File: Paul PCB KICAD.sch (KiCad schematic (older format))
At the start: 19 parts

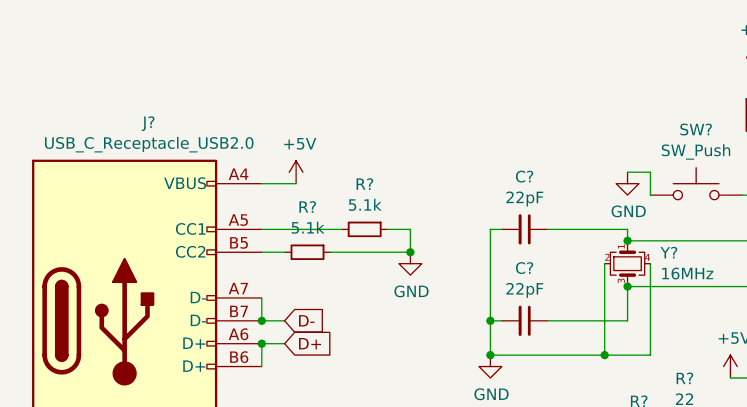
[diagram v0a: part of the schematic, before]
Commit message: Fixed +5V for USB
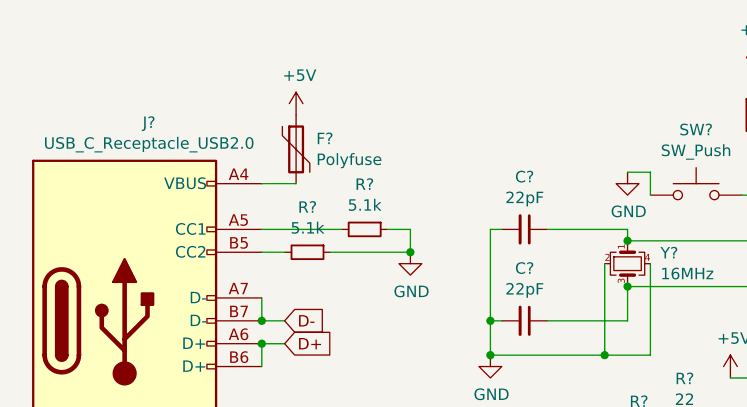
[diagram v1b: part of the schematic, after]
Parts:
- added F?: Polyfuse, symbol Device:Polyfuse
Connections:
- net +5V: now also F?.1; no longer J?.A4 (VBUS), J?.A9 (VBUS), J?.B4 (VBUS), J?.B9 (VBUS)
- new net: F?.2, J?.A4 (VBUS), J?.A9 (VBUS), J?.B4 (VBUS), J?.B9 (VBUS)
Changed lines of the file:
@@
 L power:+5V #PWR?
 U 1 1 6080295E
-P 1800 2000
-F 0 "#PWR?" H 1800 1850 50  0001 C CNN
-F 1 "+5V" H 1815 2173 50  0000 C CNN
-F 2 "" H 1800 2000 50  0001 C CNN
-F 3 "" H 1800 2000 50  0001 C CNN
-	1    1800 2000
+P 1800 1700
+F 0 "#PWR?" H 1800 1550 50  0001 C CNN
+F 1 "+5V" H 1815 1873 50  0000 C CNN
+F 2 "" H 1800 1700 50  0001 C CNN
+F 3 "" H 1800 1700 50  0001 C CNN
+	1    1800 1700
 	1    0    0    -1
 $EndComp
@@
 Wire Wire Line
 	850  4050 1100 4050
+$Comp
+L Device:Polyfuse F?
+U 1 1 607B6BD8
+P 1800 1850
+F 0 "F?" H 1888 1896 50  0000 L CNN
+F 1 "Polyfuse" H 1888 1805 50  0000 L CNN
+F 2 "" H 1850 1650 50  0001 L CNN
+F 3 "~" H 1800 1850 50  0001 C CNN
+	1    1800 1850
+	1    0    0    -1
+$EndComp
 $EndSCHEMATC

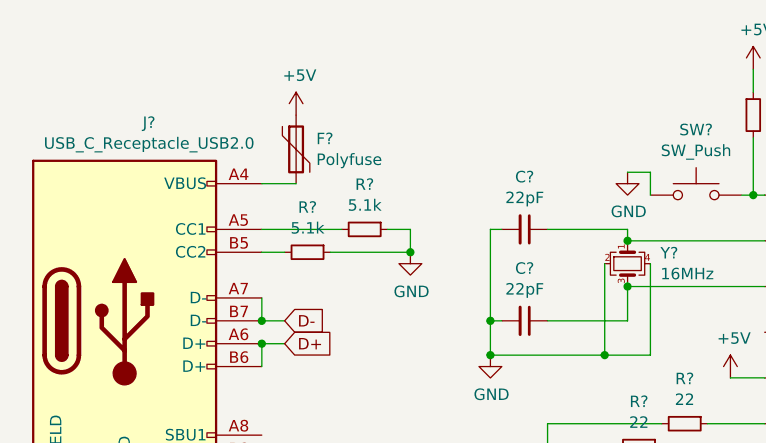
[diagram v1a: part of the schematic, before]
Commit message: Added License and fixed PolyFuse Value
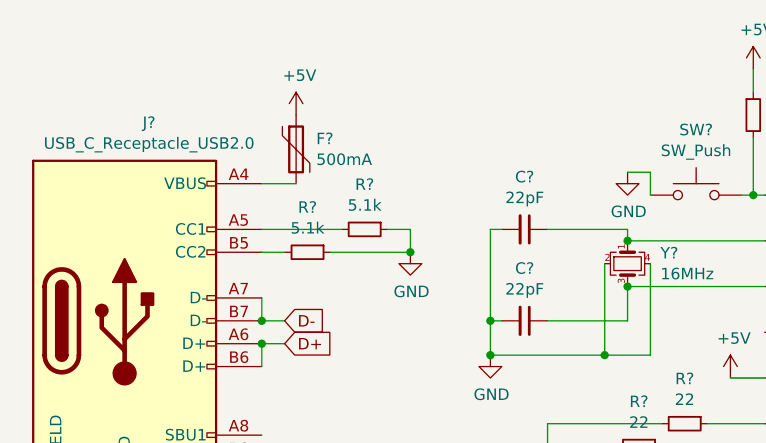
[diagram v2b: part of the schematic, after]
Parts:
- F?: value Polyfuse -> 500mA
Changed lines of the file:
@@
 P 1800 1850
 F 0 "F?" H 1888 1896 50  0000 L CNN
-F 1 "Polyfuse" H 1888 1805 50  0000 L CNN
+F 1 "500mA" H 1888 1805 50  0000 L CNN
 F 2 "" H 1850 1650 50  0001 L CNN
 F 3 "~" H 1800 1850 50  0001 C CNN

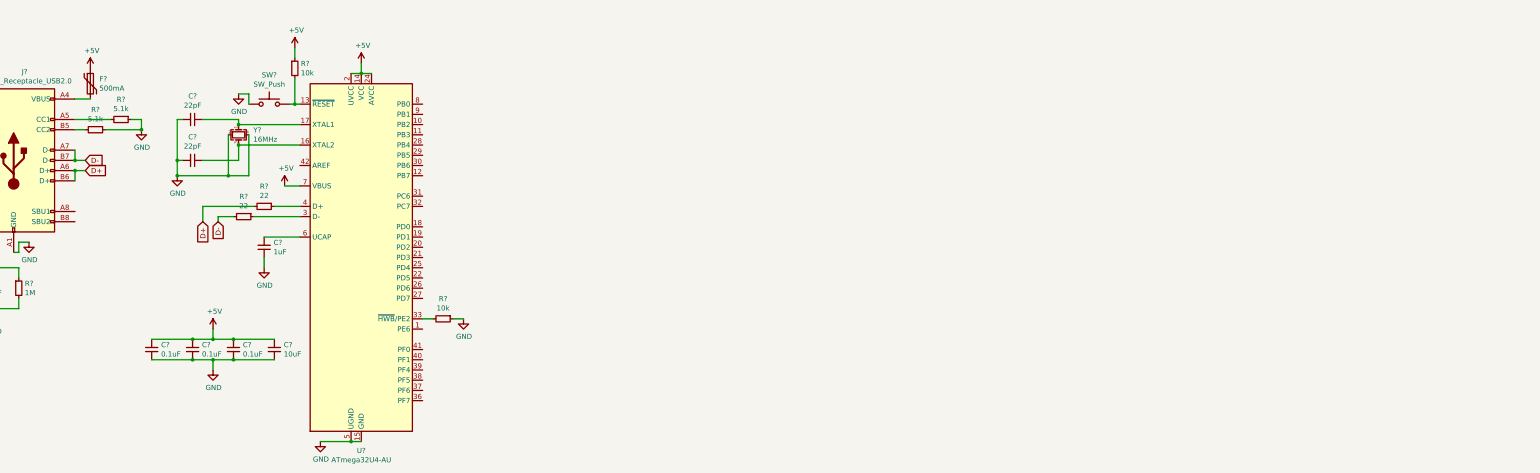
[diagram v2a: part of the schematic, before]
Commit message: Added Switch Layout to Schematic
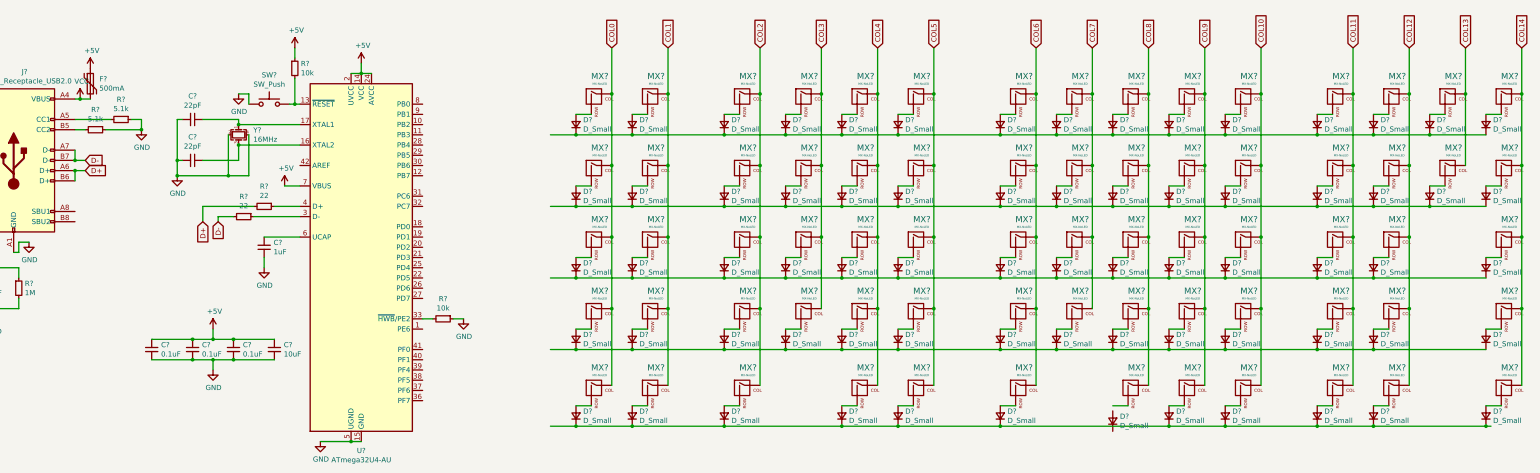
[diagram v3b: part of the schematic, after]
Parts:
- added D? (x70): D_Small, symbol Device:D_Small
- added MX? (x70): MX-NoLED, symbol MX_Alps_Hybrid:MX-NoLED
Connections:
- net VCC: now reaches F?.2, J?.A4 (VBUS), J?.A9 (VBUS), J?.B4 (VBUS), J?.B9 (VBUS)
- new net: D?.2 (A), MX?.2 (ROW) (x69)
- new net: D?.1 (K), D?.1 (K), D?.1 (K), D?.1 (K), D?.1 (K), D?.1 (K), D?.1 (K), D?.1 (K), D?.1 (K), D?.1 (K), D?.1 (K), D?.1 (K), D?.1 (K), D?.1 (K), D?.1 (K) (x2)
- new net: D?.1 (K), D?.1 (K), D?.1 (K), D?.1 (K), D?.1 (K), D?.1 (K), D?.1 (K), D?.1 (K), D?.1 (K), D?.1 (K), D?.1 (K), D?.1 (K), D?.1 (K), D?.1 (K) (x2)
- new net: D?.1 (K), D?.1 (K), D?.1 (K), D?.1 (K), D?.1 (K), D?.1 (K), D?.1 (K), D?.1 (K), D?.1 (K), D?.1 (K), D?.1 (K)
- new net COL0: MX?.1 (COL), MX?.1 (COL), MX?.1 (COL), MX?.1 (COL), MX?.1 (COL)
- new net COL1: MX?.1 (COL), MX?.1 (COL), MX?.1 (COL), MX?.1 (COL), MX?.1 (COL)
- new net COL10: MX?.1 (COL), MX?.1 (COL), MX?.1 (COL), MX?.1 (COL), MX?.1 (COL)
- new net COL11: MX?.1 (COL), MX?.1 (COL), MX?.1 (COL), MX?.1 (COL), MX?.1 (COL)
- new net COL12: MX?.1 (COL), MX?.1 (COL), MX?.1 (COL), MX?.1 (COL), MX?.1 (COL)
- new net COL13: MX?.1 (COL), MX?.1 (COL)
- new net COL14: MX?.1 (COL), MX?.1 (COL), MX?.1 (COL), MX?.1 (COL), MX?.1 (COL)
- new net COL2: MX?.1 (COL), MX?.1 (COL), MX?.1 (COL), MX?.1 (COL), MX?.1 (COL)
- new net COL3: MX?.1 (COL), MX?.1 (COL), MX?.1 (COL), MX?.1 (COL)
- new net COL4: MX?.1 (COL), MX?.1 (COL), MX?.1 (COL), MX?.1 (COL), MX?.1 (COL)
- new net COL5: MX?.1 (COL), MX?.1 (COL), MX?.1 (COL), MX?.1 (COL), MX?.1 (COL)
- new net COL6: MX?.1 (COL), MX?.1 (COL), MX?.1 (COL), MX?.1 (COL), MX?.1 (COL)
- new net COL7: MX?.1 (COL), MX?.1 (COL), MX?.1 (COL), MX?.1 (COL)
- new net COL8: MX?.1 (COL), MX?.1 (COL), MX?.1 (COL), MX?.1 (COL), MX?.1 (COL)
- new net COL9: MX?.1 (COL), MX?.1 (COL), MX?.1 (COL), MX?.1 (COL), MX?.1 (COL)

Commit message: Started Adding Footprints
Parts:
- C1, C2, C3, C4, C5, C6, C7, C8: renamed from C?; footprint (none) -> Capacitor_SMD:C_0805_2012Metric
- D1, D10, D11, D12, D13, D14, D15, D16, D17, D18, D19, D2, D20, D21, D22, D23, D24, D25, D26, D27, D28, D29, D3, D30, D31, D32, D33, D34, D35, D36, D37, D38, D39, D4, D40, D41, D42, D43, D44, D45, D46, D47, D48, D49, D5, D50, D51, D52, D53, D54, D55, D56, D57, D58, D59, D6, D60, D61, D62, D63, D64, D65, D66, D67, D68, D69, D7, D70, D8, D9: renamed from D?; footprint (none) -> Diode_SMD:D_SOD-123
- F1: renamed from F?; footprint (none) -> Fuse:Fuse_1206_3216Metric
- MX1: renamed from MX?; footprint (none) -> MX_Only:MXOnly-1U-Hotswap
- gave numbers to parts that had none: 80
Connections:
- net ROW0: now reaches D1.1 (K), D11.1 (K), D16.1 (K), D20.1 (K), D25.1 (K), D30.1 (K), D35.1 (K), D39.1 (K), D44.1 (K), D49.1 (K), D54.1 (K), D59.1 (K), D6.1 (K), D64.1 (K), D66.1 (K)
- net ROW1: now reaches D12.1 (K), D17.1 (K), D2.1 (K), D21.1 (K), D26.1 (K), D31.1 (K), D36.1 (K), D40.1 (K), D45.1 (K), D50.1 (K), D55.1 (K), D60.1 (K), D65.1 (K), D67.1 (K), D7.1 (K)
- net ROW2: now reaches D13.1 (K), D18.1 (K), D22.1 (K), D27.1 (K), D3.1 (K), D32.1 (K), D37.1 (K), D41.1 (K), D46.1 (K), D51.1 (K), D56.1 (K), D61.1 (K), D68.1 (K), D8.1 (K)
- net ROW3: now reaches D14.1 (K), D19.1 (K), D23.1 (K), D28.1 (K), D33.1 (K), D38.1 (K), D4.1 (K), D42.1 (K), D47.1 (K), D52.1 (K), D57.1 (K), D62.1 (K), D69.1 (K), D9.1 (K)
- net ROW4: now reaches D10.1 (K), D15.1 (K), D24.1 (K), D29.1 (K), D34.1 (K), D48.1 (K), D5.1 (K), D53.1 (K), D58.1 (K), D63.1 (K), D70.1 (K)

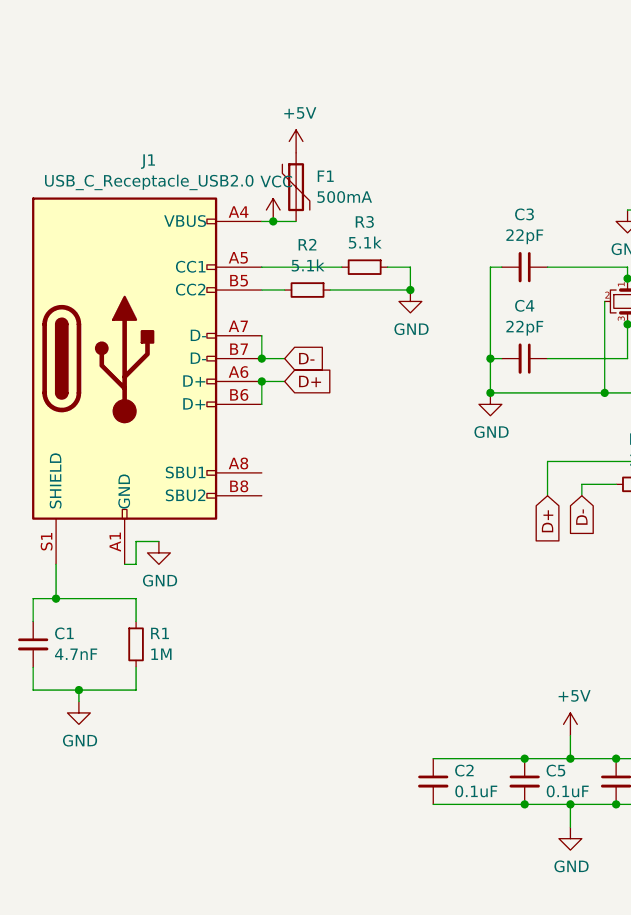
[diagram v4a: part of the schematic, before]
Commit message: Updated USB to 4084 GCT
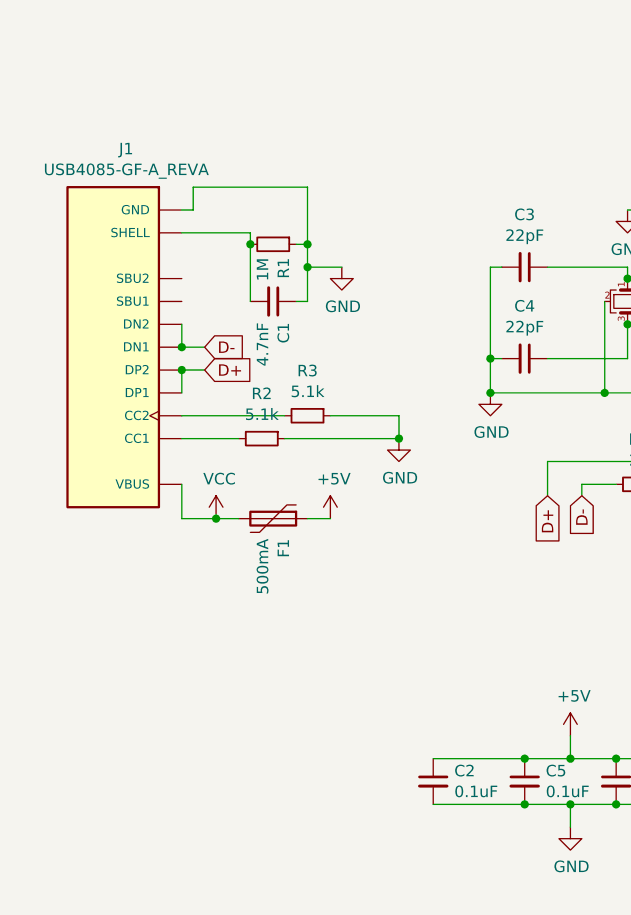
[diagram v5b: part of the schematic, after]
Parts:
- removed J1: USB_C_Receptacle_USB2.0, symbol Connector:USB_C_Receptacle_USB2.0
- added J1: USB4085-GF-A_REVA, 4085 USB Connector GCT:GCT_USB4085-GF-A_REVA, symbol USB4085-GF-A_REVA:USB4085-GF-A_REVA
- R1, R2, R3, R4, R5, R6, R7: footprint (none) -> Resistor_SMD:R_0805_2012Metric
- SW1: footprint (none) -> random-keyboard-parts:SKQG-1155865
- Y1: footprint (none) -> Crystal:Crystal_SMD_3225-4Pin_3.2x2.5mm
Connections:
- net D+: now also J1.A6 (DP1), J1.B6 (DP2)
- net D-: now also J1.A7 (DN1), J1.B7 (DN2)
- net GND: now also C1.1, R1.1, J1.A1 (GND), J1.A12 (GND), J1.B1 (GND), J1.B12 (GND); no longer C1.2, R1.2
- net VCC: now also J1.A4 (VBUS), J1.A9 (VBUS), J1.B4 (VBUS), J1.B9 (VBUS)
- net at R3.2: now also J1.B5 (CC2)
- net at R2.2: now also J1.A5 (CC1)
- new net: C1.2, J1.P1 (SHELL), J1.P2 (SHELL), J1.P3 (SHELL), J1.P4 (SHELL), R1.2
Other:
- moved on the sheet: C1, F1, R1, R2, R3
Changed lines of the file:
@@
 F 0 "R7" V 5054 4150 50  0000 C CNN
 F 1 "10k" V 5145 4150 50  0000 C CNN
-F 2 "" H 5250 4150 50  0001 C CNN
+F 2 "Resistor_SMD:R_0805_2012Metric" H 5250 4150 50  0001 C CNN
 F 3 "~" H 5250 4150 50  0001 C CNN
 	1    5250 4150
@@
 F 0 "R5" V 3304 3050 50  0000 C CNN
 F 1 "22" V 3395 3050 50  0000 C CNN
-F 2 "" H 3500 3050 50  0001 C CNN
+F 2 "Resistor_SMD:R_0805_2012Metric" H 3500 3050 50  0001 C CNN
 F 3 "~" H 3500 3050 50  0001 C CNN
 	1    3500 3050
@@
 F 0 "R4" V 3104 3150 50  0000 C CNN
 F 1 "22" V 3195 3150 50  0000 C CNN
-F 2 "" H 3300 3150 50  0001 C CNN
+F 2 "Resistor_SMD:R_0805_2012Metric" H 3300 3150 50  0001 C CNN
 F 3 "~" H 3300 3150 50  0001 C CNN
 	1    3300 3150
@@
 F 0 "Y1" V 3204 2494 50  0000 L CNN
 F 1 "16MHz" V 3295 2494 50  0000 L CNN
-F 2 "" H 3250 2350 50  0001 C CNN
+F 2 "Crystal:Crystal_SMD_3225-4Pin_3.2x2.5mm" H 3250 2350 50  0001 C CNN
 F 3 "~" H 3250 2350 50  0001 C CNN
 	1    3250 2350
@@
 F 0 "R6" H 3859 1746 50  0000 L CNN
 F 1 "10k" H 3859 1655 50  0000 L CNN
-F 2 "" H 3800 1700 50  0001 C CNN
+F 2 "Resistor_SMD:R_0805_2012Metric" H 3800 1700 50  0001 C CNN
 F 3 "~" H 3800 1700 50  0001 C CNN
 	1    3800 1700
@@
 F 0 "SW1" H 3550 2335 50  0000 C CNN
 F 1 "SW_Push" H 3550 2244 50  0000 C CNN
-F 2 "" H 3550 2250 50  0001 C CNN
+F 2 "random-keyboard-parts:SKQG-1155865" H 3550 2250 50  0001 C CNN
 F 3 "~" H 3550 2250 50  0001 C CNN
 	1    3550 2050
@@
 D-
 $Comp
-L Connector:USB_C_Receptacle_USB2.0 J1
-U 1 1 607E82B6
-P 1050 2600
-F 0 "J1" H 1157 3467 50  0000 C CNN
-F 1 "USB_C_Receptacle_USB2.0" H 1157 3376 50  0000 C CNN
-F 2 "" H 1200 2600 50  0001 C CNN
-F 3 "https://www.usb.org/sites/default/files/documents/usb_type-c.zip" H 1200 2600 50  0001 C CNN
-	1    1050 2600
-	1    0    0    -1
-$EndComp
-$Comp
 L power:GND #PWR0111
 U 1 1 607F76C2
-P 1200 3400
-F 0 "#PWR0111" H 1200 3150 50  0001 C CNN
-F 1 "GND" H 1205 3227 50  0000 C CNN
-F 2 "" H 1200 3400 50  0001 C CNN
-F 3 "" H 1200 3400 50  0001 C CNN
-	1    1200 3400
+P 2000 2200
+F 0 "#PWR0111" H 2000 1950 50  0001 C CNN
+F 1 "GND" H 2005 2027 50  0000 C CNN
+F 2 "" H 2000 2200 50  0001 C CNN
+F 3 "" H 2000 2200 50  0001 C CNN
+	1    2000 2200
 	1    0    0    -1
 $EndComp
@@
 L power:GND #PWR0112
 U 1 1 607F7AE7
-P 2300 2300
-F 0 "#PWR0112" H 2300 2050 50  0001 C CNN
-F 1 "GND" H 2305 2127 50  0000 C CNN
-F 2 "" H 2300 2300 50  0001 C CNN
-F 3 "" H 2300 2300 50  0001 C CNN
-	1    2300 2300
+P 2250 2950
+F 0 "#PWR0112" H 2250 2700 50  0001 C CNN
+F 1 "GND" H 2255 2777 50  0000 C CNN
+F 2 "" H 2250 2950 50  0001 C CNN
+F 3 "" H 2250 2950 50  0001 C CNN
+	1    2250 2950
 	1    0    0    -1
 $EndComp
@@
 L Device:R_Small R3
 U 1 1 607F8303
-P 2100 2200
-F 0 "R3" V 1904 2200 50  0000 C CNN
-F 1 "5.1k" V 1995 2200 50  0000 C CNN
-F 2 "" H 2100 2200 50  0001 C CNN
-F 3 "~" H 2100 2200 50  0001 C CNN
-	1    2100 2200
+P 1850 2850
+F 0 "R3" V 1654 2850 50  0000 C CNN
+F 1 "5.1k" V 1745 2850 50  0000 C CNN
+F 2 "Resistor_SMD:R_0805_2012Metric" H 1850 2850 50  0001 C CNN
+F 3 "~" H 1850 2850 50  0001 C CNN
+	1    1850 2850
 	0    1    1    0
 $EndComp
@@
 L Device:R_Small R2
 U 1 1 607F8861
-P 1850 2300
-F 0 "R2" V 1654 2300 50  0000 C CNN
-F 1 "5.1k" V 1745 2300 50  0000 C CNN
-F 2 "" H 1850 2300 50  0001 C CNN
-F 3 "~" H 1850 2300 50  0001 C CNN
-	1    1850 2300
+P 1650 2950
+F 0 "R2" V 1454 2950 50  0000 C CNN
+F 1 "5.1k" V 1545 2950 50  0000 C CNN
+F 2 "Resistor_SMD:R_0805_2012Metric" H 1650 2950 50  0001 C CNN
+F 3 "~" H 1650 2950 50  0001 C CNN
+	1    1650 2950
 	0    1    1    0
 $EndComp
 Wire Wire Line
-	1650 2300 1750 2300
-Wire Wire Line
-	1650 2600 1650 2500
-Wire Wire Line
-	1650 2700 1650 2800
-Wire Wire Line
-	1650 2700 1750 2700
-Connection ~ 1650 2700
-Wire Wire Line
-	1650 2600 1750 2600
-Connection ~ 1650 2600
+	1300 2950 1550 2950
+Wire Wire Line
+	1300 2550 1300 2450
+Wire Wire Line
+	1300 2650 1300 2750
+Wire Wire Line
+	1300 2650 1400 2650
+Wire Wire Line
+	1300 2550 1400 2550
 $Comp
 L power:+5V #PWR0113
 U 1 1 6080295E
-P 1800 1700
-F 0 "#PWR0113" H 1800 1550 50  0001 C CNN
-F 1 "+5V" H 1815 1873 50  0000 C CNN
-F 2 "" H 1800 1700 50  0001 C CNN
-F 3 "" H 1800 1700 50  0001 C CNN
-	1    1800 1700
-	1    0    0    -1
-$EndComp
-Wire Wire Line
-	1950 2300 2300 2300
-Wire Wire Line
-	2200 2200 2300 2200
-Wire Wire Line
-	2300 2200 2300 2300
-Connection ~ 2300 2300
-Wire Wire Line
-	1650 2200 2000 2200
-Wire Wire Line
-	1650 2000 1700 2000
-Text GLabel 1750 2700 2    50   Input ~ 0
+P 1950 3300
+F 0 "#PWR0113" H 1950 3150 50  0001 C CNN
+F 1 "+5V" H 1965 3473 50  0000 C CNN
+F 2 "" H 1950 3300 50  0001 C CNN
+F 3 "" H 1950 3300 50  0001 C CNN
+	1    1950 3300
+	1    0    0    -1
+$EndComp
+Wire Wire Line
+	1750 2950 2250 2950
+Wire Wire Line
+	1300 2850 1750 2850
+Text GLabel 1400 2650 2    50   Input ~ 0
 D+
-Text GLabel 1750 2600 2    50   Input ~ 0
+Text GLabel 1400 2550 2    50   Input ~ 0
 D-
 $Comp
 L Device:R_Small R1
 U 1 1 608109C8
-P 1100 3850
-F 0 "R1" H 1159 3896 50  0000 L CNN
-F 1 "1M" H 1159 3805 50  0000 L CNN
-F 2 "" H 1100 3850 50  0001 C CNN
-F 3 "~" H 1100 3850 50  0001 C CNN
-	1    1100 3850
-	1    0    0    -1
+P 1700 2100
+F 0 "R1" H 1759 2146 50  0000 L CNN
+F 1 "1M" H 1759 2055 50  0000 L CNN
+F 2 "Resistor_SMD:R_0805_2012Metric" H 1700 2100 50  0001 C CNN
+F 3 "~" H 1700 2100 50  0001 C CNN
+	1    1700 2100
+	0    1    1    0
 $EndComp
 $Comp
 L Device:C_Small C1
 U 1 1 6081247B
-P 650 3850
-F 0 "C1" H 742 3896 50  0000 L CNN
-F 1 "4.7nF" H 742 3805 50  0000 L CNN
-F 2 "Capacitor_SMD:C_0805_2012Metric" H 650 3850 50  0001 C CNN
-F 3 "~" H 650 3850 50  0001 C CNN
-	1    650  3850
-	1    0    0    -1
-$EndComp
-Wire Wire Line
-	1050 3500 1100 3500
-Wire Wire Line
-	1100 3500 1100 3400
-Wire Wire Line
-	1100 3400 1200 3400
-Wire Wire Line
-	750  3500 750  3650
-Wire Wire Line
-	750  3650 650  3650
-Wire Wire Line
-	650  3650 650  3750
-Wire Wire Line
-	750  3650 1100 3650
-Wire Wire Line
-	1100 3650 1100 3750
-Connection ~ 750  3650
-Wire Wire Line
-	650  3950 650  4050
-Wire Wire Line
-	1100 4050 1100 3950
-Wire Wire Line
-	650  4050 850  4050
-$Comp
-L power:GND #PWR0114
-U 1 1 6081B5AC
-P 850 4100
-F 0 "#PWR0114" H 850 3850 50  0001 C CNN
-F 1 "GND" H 855 3927 50  0000 C CNN
-F 2 "" H 850 4100 50  0001 C CNN
-F 3 "" H 850 4100 50  0001 C CNN
-	1    850  4100
-	1    0    0    -1
-$EndComp
-Wire Wire Line
-	850  4050 850  4100
-Connection ~ 850  4050
-Wire Wire Line
-	850  4050 1100 4050
+P 1700 2350
+F 0 "C1" H 1792 2396 50  0000 L CNN
+F 1 "4.7nF" H 1792 2305 50  0000 L CNN
+F 2 "Capacitor_SMD:C_0805_2012Metric" H 1700 2350 50  0001 C CNN
+F 3 "~" H 1700 2350 50  0001 C CNN
+	1    1700 2350
+	0    1    1    0
+$EndComp
+Wire Wire Line
+	1300 1950 1350 1950
+Wire Wire Line
+	1350 1950 1350 1850
 $Comp
 L Device:Polyfuse F1
 U 1 1 607B6BD8
-P 1800 1850
-F 0 "F1" H 1888 1896 50  0000 L CNN
-F 1 "500mA" H 1888 1805 50  0000 L CNN
-F 2 "Fuse:Fuse_1206_3216Metric" H 1850 1650 50  0001 L CNN
-F 3 "~" H 1800 1850 50  0001 C CNN
-	1    1800 1850
-	1    0    0    -1
+P 1700 3300
+F 0 "F1" H 1788 3346 50  0000 L CNN
+F 1 "500mA" H 1788 3255 50  0000 L CNN
+F 2 "Fuse:Fuse_1206_3216Metric" H 1750 3100 50  0001 L CNN
+F 3 "~" H 1700 3300 50  0001 C CNN
+	1    1700 3300
+	0    1    1    0
 $EndComp
 $Comp
 L power:VCC #PWR0115
 U 1 1 607DF19B
-P 1700 2000
-F 0 "#PWR0115" H 1700 1850 50  0001 C CNN
-F 1 "VCC" H 1715 2173 50  0000 C CNN
-F 2 "" H 1700 2000 50  0001 C CNN
-F 3 "" H 1700 2000 50  0001 C CNN
-	1    1700 2000
-	1    0    0    -1
-$EndComp
-Connection ~ 1700 2000
-Wire Wire Line
-	1700 2000 1800 2000
+P 1450 3300
+F 0 "#PWR0115" H 1450 3150 50  0001 C CNN
+F 1 "VCC" H 1465 3473 50  0000 C CNN
+F 2 "" H 1450 3300 50  0001 C CNN
+F 3 "" H 1450 3300 50  0001 C CNN
+	1    1450 3300
+	1    0    0    -1
+$EndComp
+Connection ~ 1450 3300
+Wire Wire Line
+	1450 3300 1550 3300
 $Comp
 L MX_Alps_Hybrid:MX-NoLED MX1
@@
 Text GLabel 6300 5200 0    50   Input ~ 0
 ROW4
+$Comp
+L USB4085-GF-A_REVA:USB4085-GF-A_REVA J1
+U 1 1 607FE1B5
+P 1000 2550
+F 0 "J1" H 943 1683 50  0000 C CNN
+F 1 "USB4085-GF-A_REVA" H 943 1774 50  0000 C CNN
+F 2 "4085 USB Connector GCT:GCT_USB4085-GF-A_REVA" H 1000 2550 50  0001 L BNN
+F 3 "" H 1000 2550 50  0001 L BNN
+F 4 "Manufacturer Recommendations" H 1000 2550 50  0001 L BNN "STANDARD"
+F 5 "Global Connector Technology" H 1000 2550 50  0001 L BNN "MANUFACTURER"
+F 6 "3.46mm" H 1000 2550 50  0001 L BNN "MAXIMUM_PACKAGE_HEIGHT"
+F 7 "A2" H 1000 2550 50  0001 L BNN "PARTREV"
+	1    1000 2550
+	-1   0    0    1
+$EndComp
+Wire Wire Line
+	1850 3300 1950 3300
+Connection ~ 1300 2550
+Connection ~ 1300 2650
+Wire Wire Line
+	1300 3150 1300 3300
+Wire Wire Line
+	1300 3300 1450 3300
+Wire Wire Line
+	2250 2850 2250 2950
+Wire Wire Line
+	1950 2850 2250 2850
+Connection ~ 2250 2950
+Wire Wire Line
+	1300 2050 1600 2050
+Wire Wire Line
+	1600 2050 1600 2100
+Wire Wire Line
+	1800 2350 1850 2350
+Wire Wire Line
+	1850 2350 1850 2200
+Wire Wire Line
+	1350 1850 1850 1850
+Connection ~ 1850 2200
+Wire Wire Line
+	1850 1850 1850 2100
+Wire Wire Line
+	1850 2200 2000 2200
+Connection ~ 1600 2100
+Wire Wire Line
+	1800 2100 1850 2100
+Wire Wire Line
+	1600 2100 1600 2350
+Connection ~ 1850 2100
+Wire Wire Line
+	1850 2100 1850 2200
 $EndSCHEMATC
